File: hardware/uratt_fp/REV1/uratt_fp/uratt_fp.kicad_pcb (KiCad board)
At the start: 2 copper layers, 50 x 24 mm, 27 parts, among them J1 Conn_01x10, Q1 DMP31D0U, Q2 2N7002, SW1 SW_Push

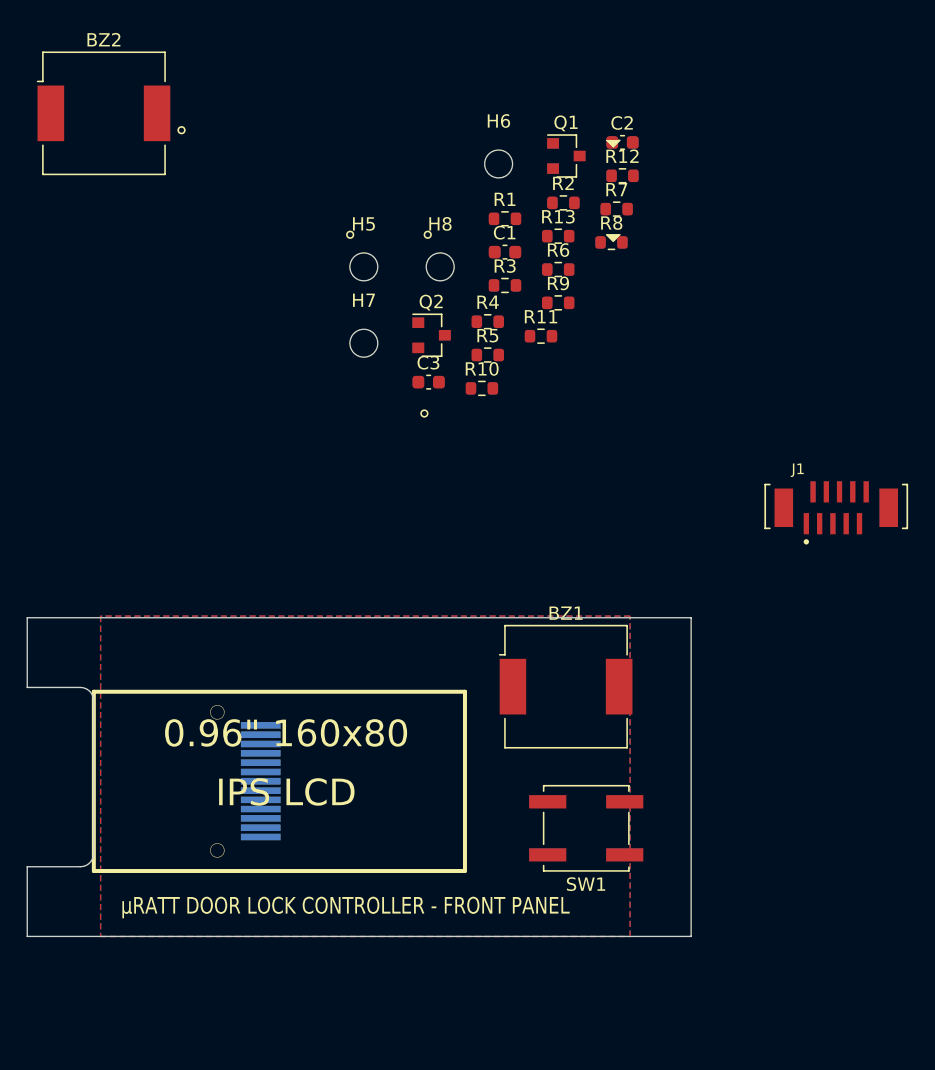
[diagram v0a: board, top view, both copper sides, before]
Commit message: separate front panel board layout
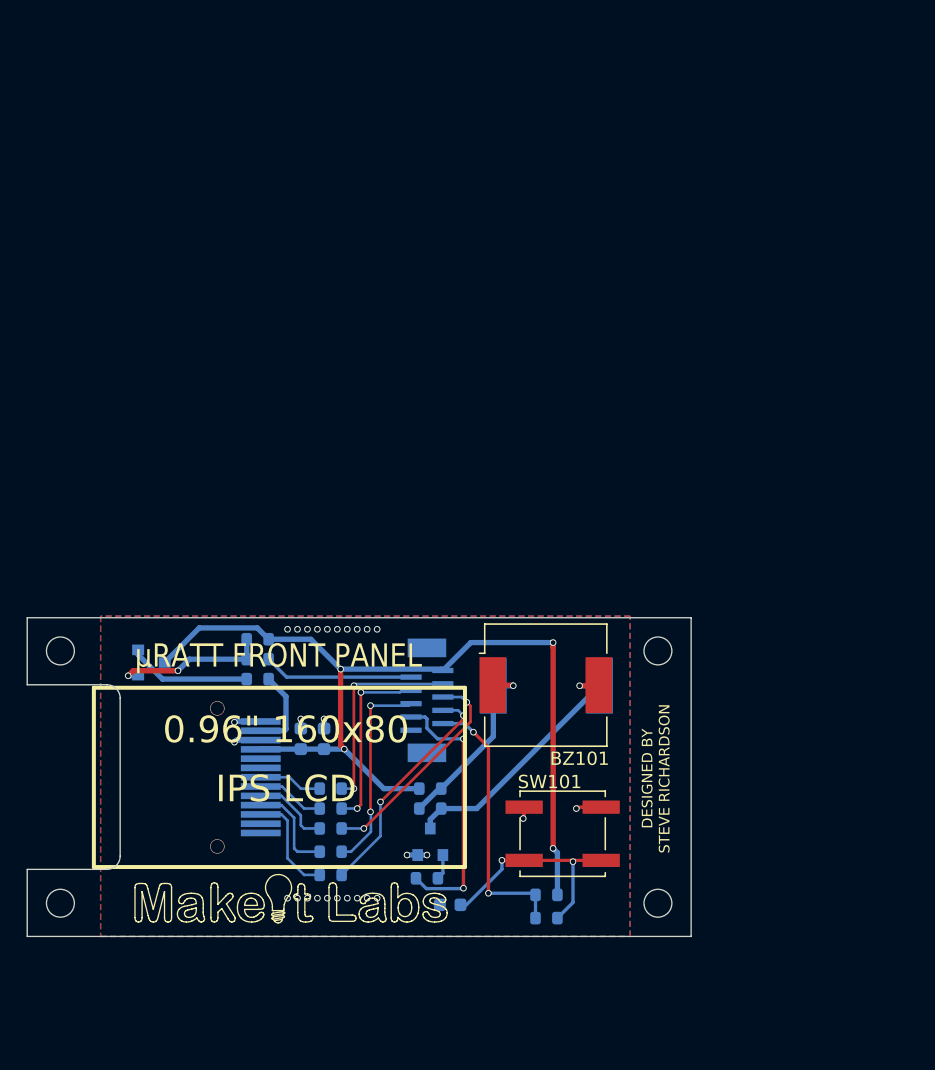
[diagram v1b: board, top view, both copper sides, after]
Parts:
- removed LCD1: ER-TFT0.96-1, uratt_fp:ER-TFT0.96-1
- added LCD101: ER-TFT0.96-1, uratt_fp:ER-TFT0.96-1, B.Cu at (42.2, 145.2)
- BZ102: renamed from BZ2; moved to B.Cu
- C101: renamed from C1; moved to B.Cu
- C102: renamed from C2; moved to B.Cu
- C103: renamed from C3; moved to B.Cu
- J101: renamed from J1; moved to B.Cu
- Q101: renamed from Q1; moved to B.Cu
- Q102: renamed from Q2; moved to B.Cu
- R101: renamed from R1; moved to B.Cu
- R102: renamed from R2; moved to B.Cu
- R103: renamed from R3; moved to B.Cu
- R104: renamed from R4; moved to B.Cu
- R105: renamed from R5; moved to B.Cu
- R106: renamed from R6; moved to B.Cu
- R107: renamed from R7; moved to B.Cu
- R108: renamed from R8; moved to B.Cu
- R109: renamed from R9; moved to B.Cu
- R110: renamed from R10; moved to B.Cu
- R111: renamed from R11; moved to B.Cu
- R112: renamed from R12; moved to B.Cu
- R113: renamed from R13; moved to B.Cu
- moved H104 55.8 mm to (39.6, 147.9)
- moved R112 54.9 mm to (67.2, 146.0), turned to 180 degrees
- moved BZ102 54.5 mm to (76.2, 131.5)
- moved R101 52.8 mm to (76.2, 149.0)
- moved R102 52.1 mm to (76.2, 147.2), turned to 180 degrees
- moved C102 51.0 mm to (57.8, 135.5), turned to 90 degrees
- moved H102 49.3 mm to (39.6, 128.9)
- moved C101 49.3 mm to (69.0, 148.0), turned to 180 degrees
- moved Q101 49.3 mm to (46.5, 129.8)
- moved R108 48.9 mm to (60.0, 142.2)
- moved R107 48.7 mm to (60.0, 139.2)
- moved H103 47.6 mm to (84.6, 147.9)
- moved R106 47.1 mm to (60.0, 144.0)
- moved R109 46.4 mm to (60.0, 145.8)
- moved R113 42.7 mm to (67.5, 139.2)
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- renumbered BZ1 to BZ101, H5 to H101, H6 to H102, H7 to H103, H8 to H104, SW1 to SW101
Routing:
- net /R_LCD_3.3V: track 0.00 -> 71.0 mm, vias 0 -> 4
- net Net-(BZ101-Pad2): track 0.00 -> 20.6 mm, vias 0 -> 1
- net /R_BTN: track 0.00 -> 20.5 mm, vias 0 -> 2
- net /R_BEEPER: track 0.00 -> 20.2 mm, vias 0 -> 2
- net /R_LCD_MOSI: track 0.00 -> 17.5 mm, vias 0 -> 2
- net Net-(C101-Pad1): track 0.00 -> 17.2 mm, vias 0 -> 2
- net /R_LCD_DC: track 0.00 -> 16.6 mm, vias 0 -> 2
- net /R_LCD_CLK: track 0.00 -> 15.5 mm, vias 0 -> 2
- net /R_LCD_CS: track 0.00 -> 15.4 mm, vias 0 -> 2
- net Net-(BZ101-Pad1): track 0.00 -> 14.7 mm, vias 0 -> 1
- net /R_LCD_RESET: track 0.00 -> 13.9 mm, vias 0 -> 2
- net Net-(Q101-Pad1): track 0.00 -> 11.7 mm, vias 0 -> 2
- net /R_LCD_BL: track 0.00 -> 11.3 mm
- net GND1: track 0.00 -> 9.81 mm, vias 0 -> 18
- net Net-(Q101-Pad2): track 0.00 -> 9.30 mm
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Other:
- outline, holes or cut-outs redrawn
- board text added: "DESIGNED BY STEVE RICHARDSON"
- board text added: "REV 1 / 2021-JAN-16"
- board text added: "µRATT FRONT PANEL"
- board text removed: "REV 0 / 2020-DEC-22"
- board text removed: "µRATT DOOR LOCK CONTROLLER - FRONT PANEL"

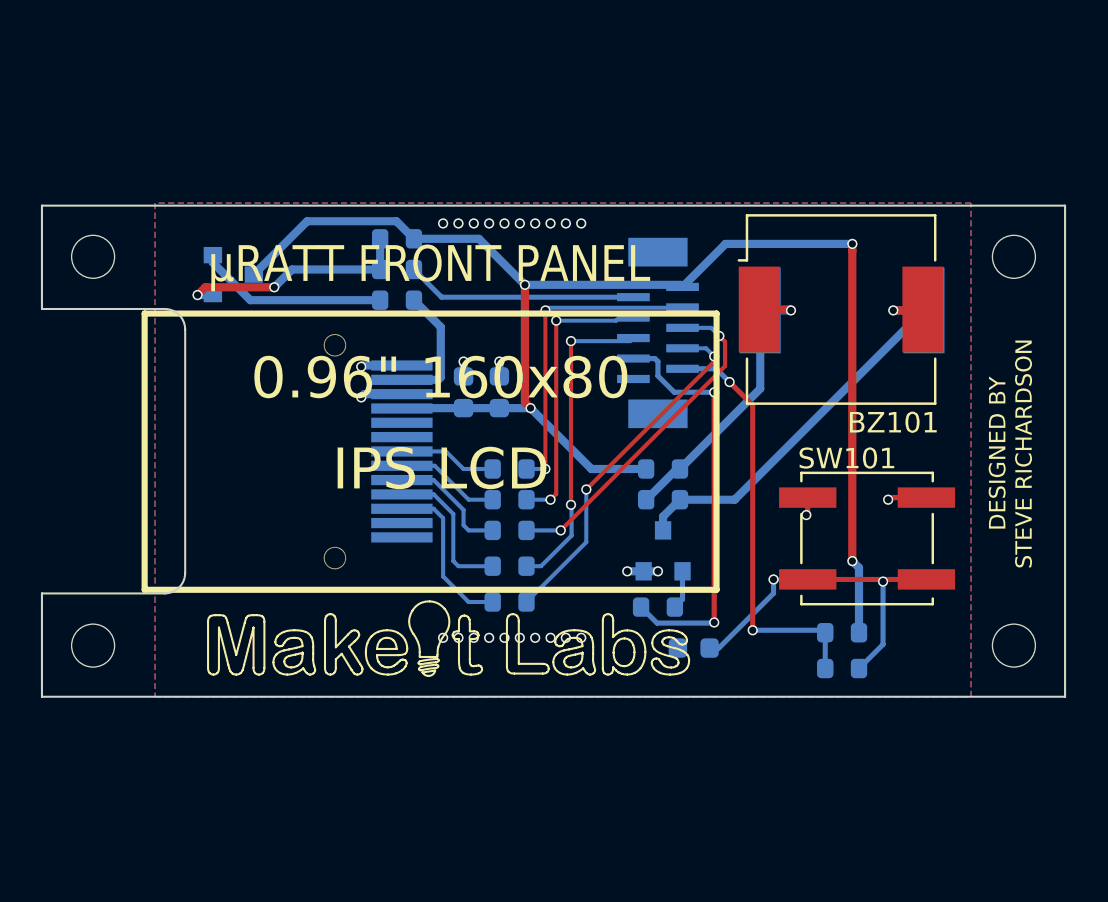
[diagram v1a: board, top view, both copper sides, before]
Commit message: uratt fp, add rails, fiducials, alt speaker option, cap, nearly ready for fab
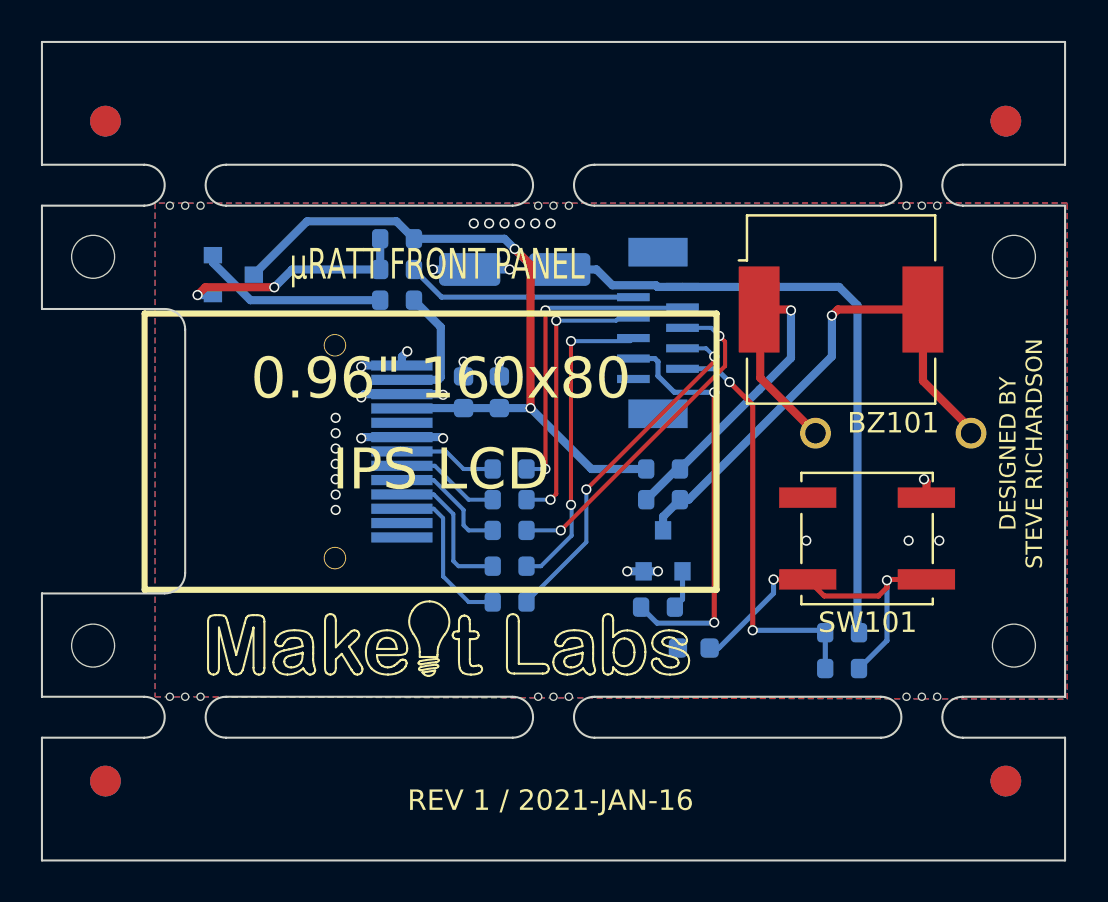
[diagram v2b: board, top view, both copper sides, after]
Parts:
- removed BZ102: Buzzer, Buzzer_Beeper:Buzzer_CUI_CPT-9019S-SMT
- added BK1: BREAKAWAY, uratt_fp:RATT_BITE, F.Cu at (42.1, 150.4)
- added BK2: BREAKAWAY, uratt_fp:RATT_BITE, F.Cu at (60.1, 150.4)
- added BK3: BREAKAWAY, uratt_fp:RATT_BITE, F.Cu at (78.1, 150.4)
- added BK4: BREAKAWAY, uratt_fp:RATT_BITE, F.Cu at (46.1, 126.4)
- added BK5: BREAKAWAY, uratt_fp:RATT_BITE, F.Cu at (64.1, 126.4)
- added BK6: BREAKAWAY, uratt_fp:RATT_BITE, F.Cu at (82.1, 126.4)
- added C104: 100uF, Capacitor_SMD:CP_Elec_5x3, B.Cu at (60.2, 129.5)
- added FID1: Fiducial, Fiducial:Fiducial_1.5mm_Mask3mm, F.Cu at (40.2, 154.5)
- added FID2: Fiducial, Fiducial:Fiducial_1.5mm_Mask3mm, F.Cu at (84.2, 154.5)
- added FID3: Fiducial, Fiducial:Fiducial_1.5mm_Mask3mm, B.Cu at (40.2, 154.5)
- added FID4: Fiducial, Fiducial:Fiducial_1.5mm_Mask3mm, B.Cu at (84.2, 154.5)
- added FID5: Fiducial, Fiducial:Fiducial_1.5mm_Mask3mm, F.Cu at (40.2, 122.2)
- added FID6: Fiducial, Fiducial:Fiducial_1.5mm_Mask3mm, F.Cu at (84.2, 122.2)
- added FID7: Fiducial, Fiducial:Fiducial_1.5mm_Mask3mm, B.Cu at (40.2, 122.2)
- added FID8: Fiducial, Fiducial:Fiducial_1.5mm_Mask3mm, B.Cu at (84.2, 122.2)
- added LS101: Speaker, uratt_fp:SPKR_CVS-1508, B.Cu at (78.8, 137.5)
- BZ101: value Buzzer (ALT) -> Buzzer
- R110: value 20 -> 15
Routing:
- net GND1: track 9.81 -> 18.6 mm, vias 18 -> 29
- net Net-(BZ101-Pad1): track 14.7 -> 21.0 mm
- net Net-(BZ101-Pad2): track 20.6 -> 25.8 mm
- net /R_LCD_3.3V: track 71.0 -> 69.6 mm, vias 4 -> 2
- net Net-(C101-Pad1): track 17.2 -> 18.1 mm
- net (no net): vias 10 -> 0
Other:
- board size 50 x 24 mm -> 50 x 40 mm

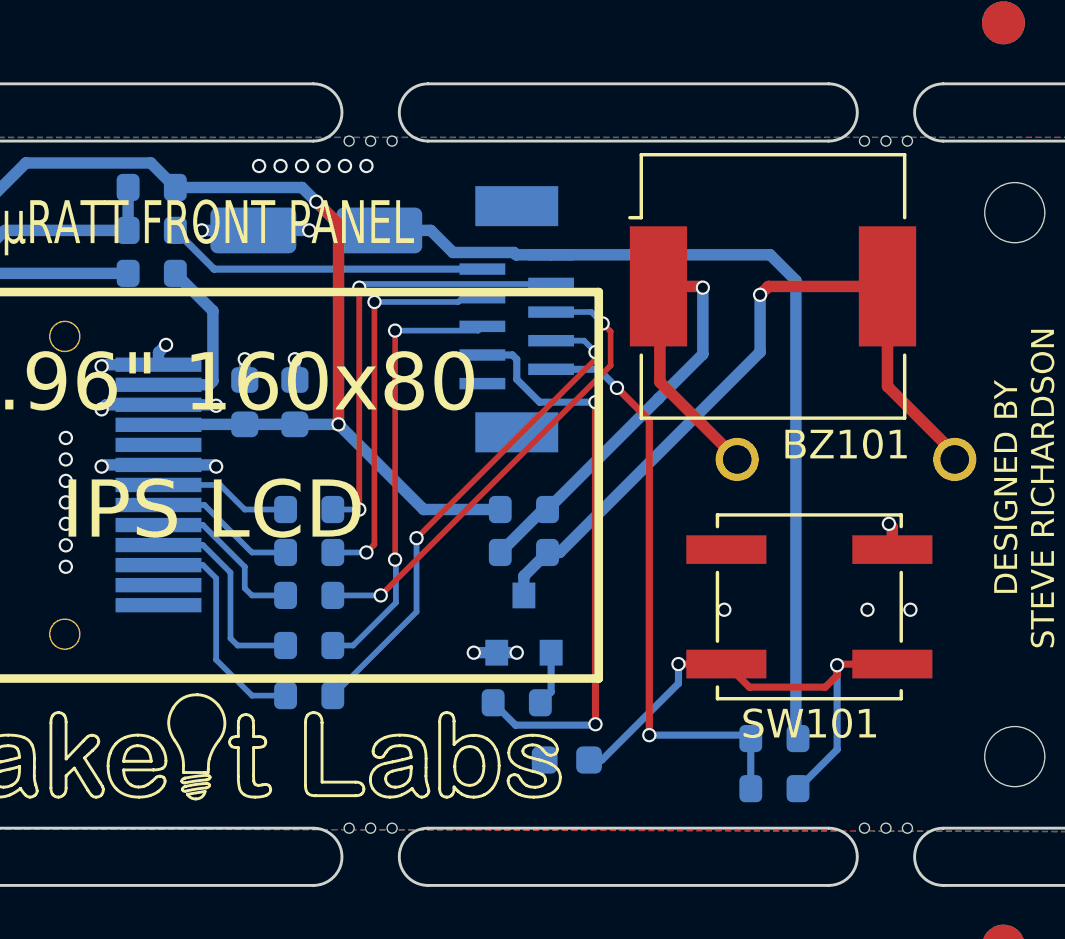
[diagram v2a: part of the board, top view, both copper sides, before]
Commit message: change front panel to 12 pin
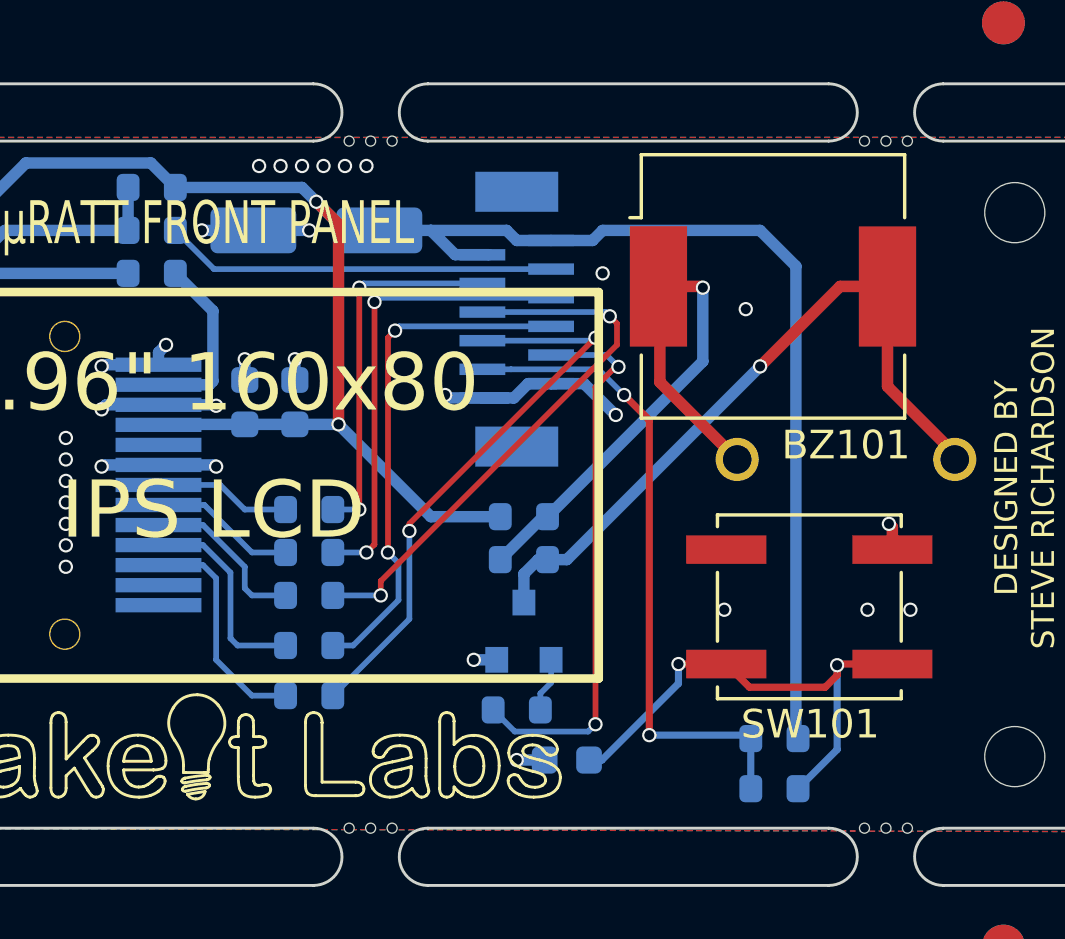
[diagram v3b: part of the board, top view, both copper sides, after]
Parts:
- J101: footprint uratt_fp:TE_1-1734742-0 -> uratt_fp:TE_1-1734742-2
- moved Q102 0.25 mm to (67.5, 143.5)
- moved R111 0.25 mm to (67.5, 141.0)
- moved R112 0.25 mm to (67.2, 146.2)
- moved R113 0.25 mm to (67.5, 139.5)
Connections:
- J101 pad 10: GND1 -> /R_BTN
- J101 pad 2: /R_LCD_BL -> /R_LCD_3.3V
- J101 pad 3: /R_LCD_CS -> /R_LCD_BL
- J101 pad 4: /R_LCD_RESET -> /R_LCD_CS
- J101 pad 5: /R_LCD_DC -> /R_LCD_RESET
- J101 pad 6: /R_LCD_CLK -> /R_LCD_DC
- J101 pad 7: /R_LCD_MOSI -> /R_LCD_CLK
- J101 pad 8: /R_BEEPER -> /R_LCD_MOSI
- J101 pad 9: /R_BTN -> /R_BEEPER
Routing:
- net GND1: track 18.6 -> 26.6 mm, vias 29 -> 33
- net /R_LCD_3.3V: track 69.6 -> 72.6 mm
- net /R_LCD_DC: track 16.6 -> 19.5 mm
- net /R_LCD_MOSI: track 17.5 -> 20.3 mm
- net /R_LCD_CLK: track 15.5 -> 18.1 mm
- net /R_BTN: track 20.5 -> 22.9 mm
- net /R_LCD_RESET: track 13.9 -> 16.3 mm
- net /R_LCD_CS: track 15.4 -> 13.0 mm
- net /R_LCD_BL: track 11.3 -> 13.7 mm
- net Net-(BZ101-Pad2): track 25.8 -> 24.9 mm
- net /R_BEEPER: track 20.2 -> 19.4 mm
